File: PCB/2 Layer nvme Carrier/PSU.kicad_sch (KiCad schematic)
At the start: 176 parts, among them J5 Barrel_Jack_Switch, J79 Conn_01x02_Pin, J80 Conn_01x02_Pin, Q5 2N7002, Q6 2N7002, Q7 NCE30P28Q, Q8 2N7002, SW1 SW_Push, SW2 SW_Push, U13 TL431DBZ, U15 SY8253ADC, U16 SY8253ADC, U400 SY8253ADC, U410 SY8253ADC, U420 SY8253ADC, U430 SY8253ADC, U440 SY8253ADC, U450 SY8253ADC, U460 SY8253ADC, U470 SY8253ADC

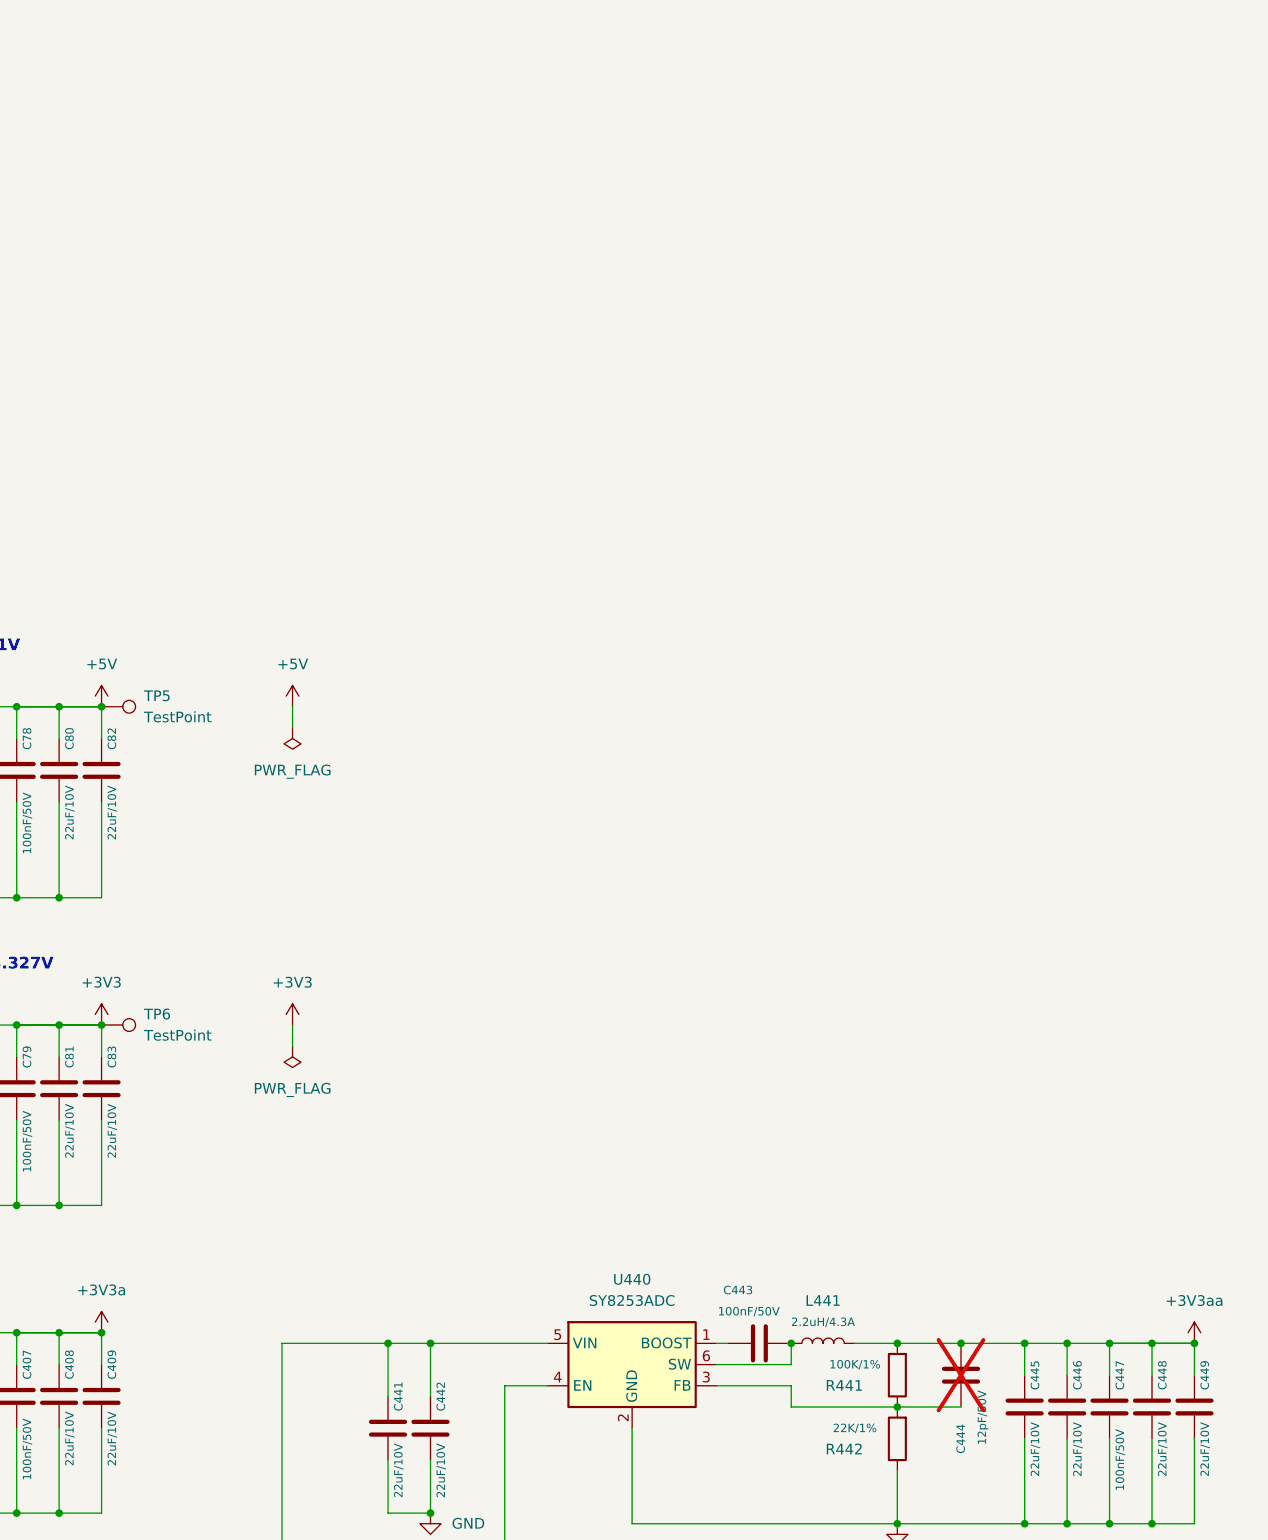
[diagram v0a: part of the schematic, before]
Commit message: Parts change for BOM
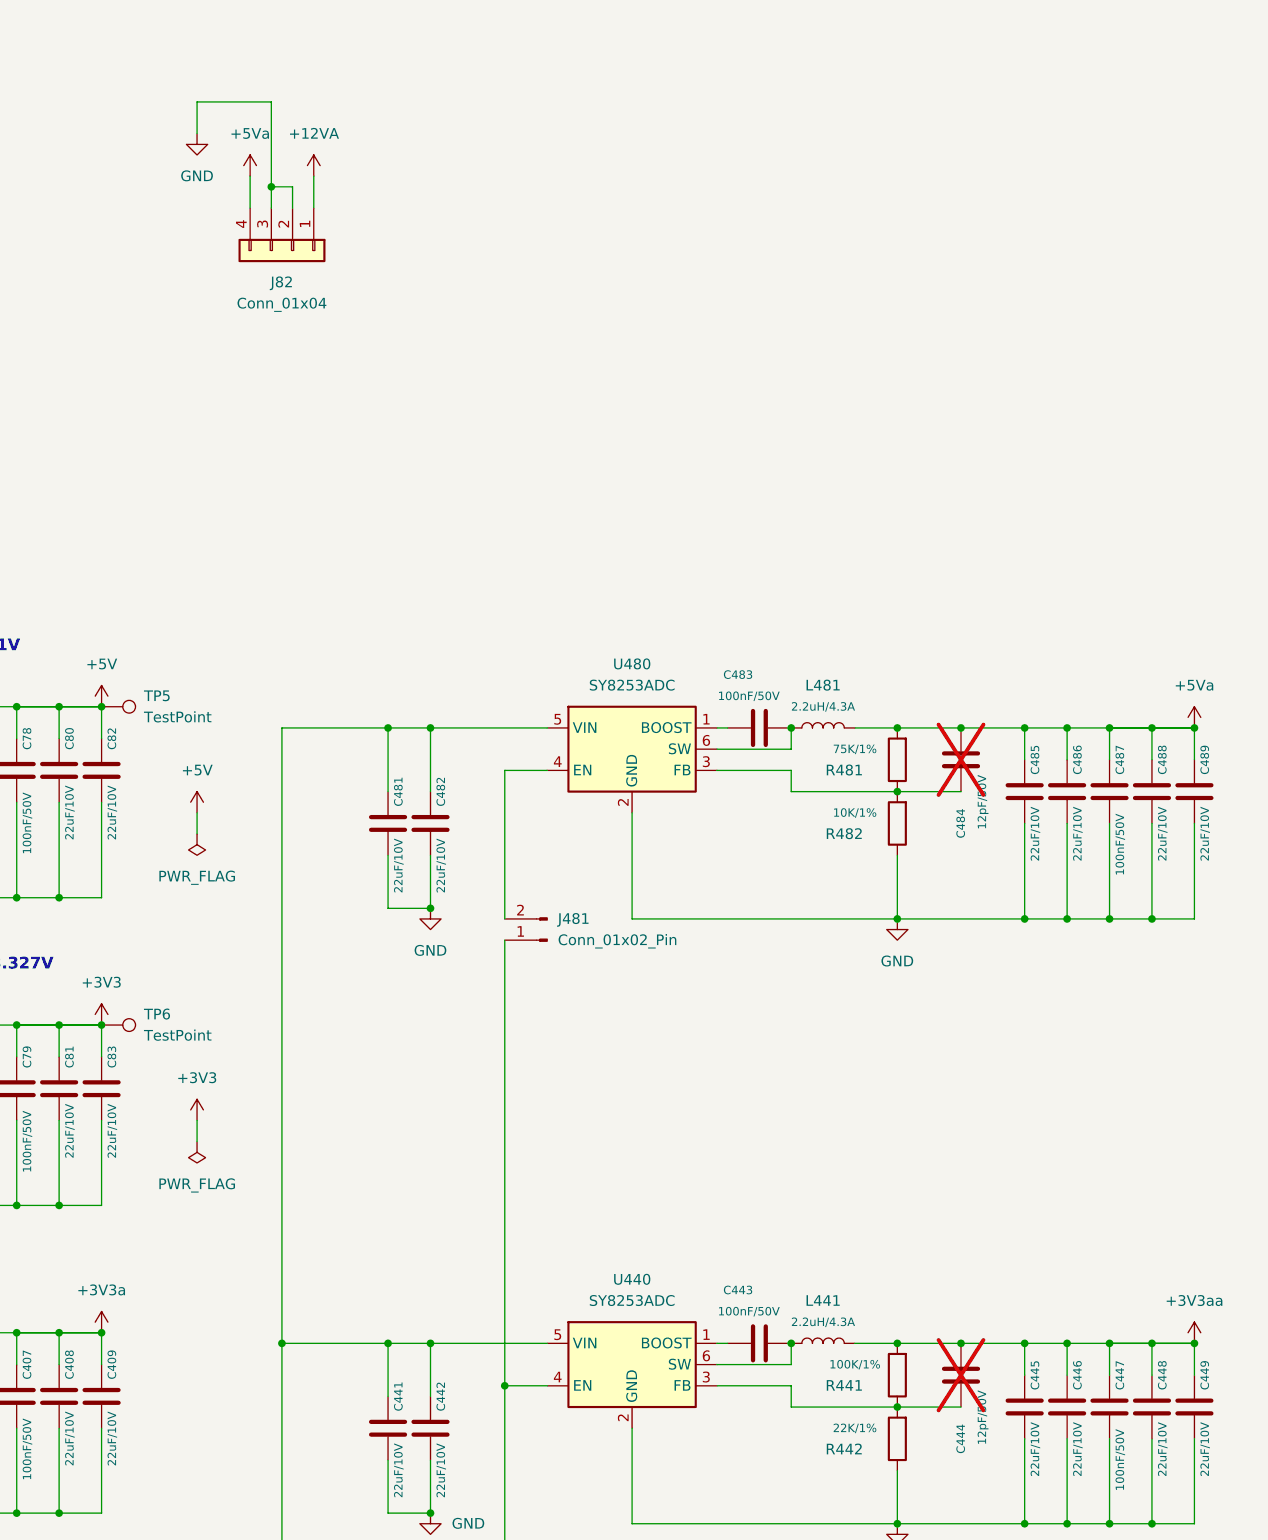
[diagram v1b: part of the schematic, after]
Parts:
- added C481, C482, C485, C486, C488, C489: 22uF/10V, A_HDJ_Library:C_0603_1608Metric, symbol Device:C
- added C483, C487: 100nF/50V, A_HDJ_Library:C_0402_1005Metric, symbol Device:C
- added C484: 12pF/50V, Capacitor_SMD:C_0402_1005Metric, symbol Device:C
- added J481: Conn_01x02_Pin, Connector_PinHeader_2.54mm:PinHeader_1x02_P2.54mm_Vertical, symbol Connector:Conn_01x02_Pin
- added J82: Conn_01x04, Connector_TE-Connectivity:TE_MATE-N-LOK_350211-1_1x04_P5.08mm_Vertical, symbol Connector_Generic:Conn_01x04
- added L481: 2.2uH/4.3A, A_HDJ_Library:L_Sunlord_SWPA4020S, symbol Device:L
- added R481: 75K/1%, A_HDJ_Library:R_0402_1005Metric, symbol Device:R
- added R482: 10K/1%, A_HDJ_Library:R_0402_1005Metric, symbol Device:R
- added U480: SY8253ADC, A_HDJ_Library:TSOT-23-6, symbol Regulator_Switching:LM2734X
- C401, C402, C405, C406, C408, C409, C411, C412, C415, C416, C418, C419, C421, C422, C425, C426, C428, C429, C431, C432, C435, C436, C438, C439, C441, C442, C445, C446, C448, C449, C451, C452, C455, C456, C458, C459, C461, C462, C465, C466, C468, C469, C64, C65, C67, C68, C74, C75, C76, C77, C80, C81, C82, C83: Mfr.# (none) -> CL10A226MP8NUNE
- C403, C407, C413, C417, C423, C427, C433, C437, C443, C447, C453, C457, C463, C467, C70, C71, C78, C79: Mfr.# (none) -> GRM155R71H104KE14D
- C62, C63, C66, C69: Mfr.# (none) -> CL05A105KO5NNNC
- D15, D16, D17: Mfr.# (none) -> SS54
- D21, D25: Mfr.# (none) -> ESD5V0B03-1006
- D22, D23: Mfr.# (none) -> SZYY0603YG
- D24: Mfr.# (none) -> MMS3Z3B3GW
- J5: Mfr.# (none) -> DC007B-2.5-J
- J79, J80: Mfr.# (none) -> 2.54-1*2
- JP1: Mfr.# (none) -> 2.54-1*3
- L1, L2, L401, L411, L421, L431, L441, L451, L461: Mfr.# (none) -> WPN4020H2R2MT
- Q5, Q6, Q8: Mfr.# (none) -> NDS7002A
- Q7: Mfr.# (none) -> NCE30P28Q
- R38, R40, R49, R58: Mfr.# (none) -> RC0402FR-0710KL
- R39, R52, R53: Mfr.# (none) -> RC0402FR-072K2L
- R401, R411, R421, R431, R44, R441, R45, R451, R461, R51, R59: Mfr.# (none) -> RC0402FR-07100KL
- R402, R412, R422, R432, R442, R452, R462, R60: Mfr.# (none) -> RC0402FR-0722KL
- R41, R42, R54: Mfr.# (none) -> RC0402FR-0721K5L
- R46, R48, R55: Mfr.# (none) -> RC0402FR-07100RL
- R47: Mfr.# (none) -> RC0402FR-071KL
- R57: Mfr.# (none) -> RC0402FR-0775KL
- SW1, SW2: Mfr.# (none) -> K2-1102SP-E3SC-04
- U13: Mfr.# (none) -> TL431DBZ
- U15, U16, U400, U410, U420, U430, U440, U450, U460: Mfr.# (none) -> SY8253ADC
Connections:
- net +12VA: now also J82.1 (Pin_1)
- net GND: now also C481.1, C482.1, C485.1, C486.1, C487.2, C488.1, C489.1, J82.2 (Pin_2), J82.3 (Pin_3), R482.1, U480.2 (GND)
- net PWR_EN: now also J481.1 (Pin_1)
- net VDC: now also C481.2, C482.2, U480.5 (VIN)
- new net: C484.2, R481.1, R482.2, U480.3 (FB)
- new net: C483.2, U480.1 (BOOST)
- new net: J481.2 (Pin_2), U480.4 (EN)
- new net: C483.1, L481.1, U480.6 (SW)
- new net +5Va: C484.1, C485.2, C486.2, C487.1, C488.2, C489.2, J82.4 (Pin_4), L481.2, R481.2

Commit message: BOM update and pdf
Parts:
- C401, C402, C405, C406, C408, C409, C411, C412, C415, C416, C418, C419, C421, C422, C425, C426, C428, C429, C431, C432, C435, C436, C438, C439, C441, C442, C445, C446, C448, C449, C451, C452, C455, C456, C458, C459, C461, C462, C465, C466, C468, C469, C481, C482, C485, C486, C488, C489, C64, C65, C67, C68, C74, C75, C76, C77, C80, C81, C82, C83: MPN (none) -> CL10A226MP8NUNE; Mfr.# CL10A226MP8NUNE -> (none)
- C403, C407, C413, C417, C423, C427, C433, C437, C443, C447, C453, C457, C463, C467, C483, C487, C70, C71, C78, C79: MPN (none) -> GRM155R71H104KE14D; Mfr.# GRM155R71H104KE14D -> (none)
- C62, C63, C66, C69: MPN (none) -> CL05A105KO5NNNC; Mfr.# CL05A105KO5NNNC -> (none)
- D15, D16, D17: MPN (none) -> SS54; Mfr.# SS54 -> (none)
- D21, D25: MPN (none) -> ESD5V0B03-1006; Mfr.# ESD5V0B03-1006 -> (none)
- D22, D23: MPN (none) -> SZYY0603YG; Mfr.# SZYY0603YG -> (none)
- D24: MPN (none) -> MMS3Z3B3GW; Mfr.# MMS3Z3B3GW -> (none)
- J481, J79, J80: MPN (none) -> 2.54-1*2; Mfr.# 2.54-1*2 -> (none)
- J5: MPN (none) -> DC007B-2.5-J; Mfr.# DC007B-2.5-J -> (none)
- J82: MPN (none) -> 770997-1; Mfr.# 770997-1 -> (none)
- JP1: MPN (none) -> 2.54-1*3; Mfr.# 2.54-1*3 -> (none)
- L1, L2, L401, L411, L421, L431, L441, L451, L461, L481: MPN (none) -> WPN4020H2R2MT; Mfr.# WPN4020H2R2MT -> (none)
- Q5, Q6, Q8: MPN (none) -> NDS7002A; Mfr.# NDS7002A -> (none)
- Q7: MPN (none) -> NCE30P28Q; Mfr.# NCE30P28Q -> (none)
- R38, R40, R482, R49, R58: MPN (none) -> RC0402FR-0710KL; Mfr.# RC0402FR-0710KL -> (none)
- R39, R52, R53: MPN (none) -> RC0402FR-072K2L; Mfr.# RC0402FR-072K2L -> (none)
- R401, R411, R421, R431, R44, R441, R45, R451, R461, R51, R59: MPN (none) -> RC0402FR-07100KL; Mfr.# RC0402FR-07100KL -> (none)
- R402, R412, R422, R432, R442, R452, R462, R60: MPN (none) -> RC0402FR-0722KL; Mfr.# RC0402FR-0722KL -> (none)
- R41, R42, R54: MPN (none) -> RC0402FR-0721K5L; Mfr.# RC0402FR-0721K5L -> (none)
- R46, R48, R55: MPN (none) -> RC0402FR-07100RL; Mfr.# RC0402FR-07100RL -> (none)
- R47: MPN (none) -> RC0402FR-071KL; Mfr.# RC0402FR-071KL -> (none)
- R481, R57: MPN (none) -> RC0402FR-0775KL; Mfr.# RC0402FR-0775KL -> (none)
- SW1, SW2: MPN (none) -> K2-1102SP-E3SC-04; Mfr.# K2-1102SP-E3SC-04 -> (none)
- U13: MPN (none) -> TL431DBZ; Mfr.# TL431DBZ -> (none)
- U15, U16, U400, U410, U420, U430, U440, U450, U460, U480: MPN (none) -> SY8253ADC; Mfr.# SY8253ADC -> (none)

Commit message: Rework for PSU and REFCLK
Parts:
- removed C62, C63: 1uF/16V, A_HDJ_Library:C_0402_1005Metric, symbol Device:C
- removed D15, D16, D17: SS54, A_HDJ_Library:D_SMA, symbol Device:D_Schottky
- removed JP1: Jumper_3_Bridged12, A_HDJ_Library:PinHeader_1x03_P2.54mm_Vertical, symbol Jumper:Jumper_3_Bridged12
- removed Q5, Q6: 2N7002, A_HDJ_Library:SOT-23, symbol Transistor_FET:2N7002
- removed Q7: NCE30P28Q, A_HDJ_Library:MOSFET_PDFN8_3.3x3.3, symbol A_HDJ_Library:AON7262E
- removed R38, R40: 10K/1%, A_HDJ_Library:R_0402_1005Metric, symbol Device:R
- removed R39: 2.2K/1%, A_HDJ_Library:R_0402_1005Metric, symbol Device:R
- removed R41, R42: 21.5K/1%, A_HDJ_Library:R_0402_1005Metric, symbol Device:R
- removed R44, R45: 100K/1%, A_HDJ_Library:R_0402_1005Metric, symbol Device:R
- removed TP8, TP9: TestPoint, A_HDJ_Library:TestPoint_Pad_D1.5mm, symbol Connector:TestPoint
- removed U13: TL431DBZ, A_HDJ_Library:SOT-23, symbol Reference_Voltage:TL431DBZ
- added D81: PTVS12VP1UP, Diode_SMD_AKL:D_SOD-128, symbol PCM_Diode_TVS_AKL:PTVS12VP1UP
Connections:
- net +12VA is gone; now on net +12V: J82.1 (Pin_1), R54.1
- net VDC is gone; now on net +12V: C401.2, C402.2, C411.2, C412.2, C421.2, C422.2, C431.2, C432.2, C441.2, C442.2, C451.2, C452.2, C461.2, C462.2, C471.2, C472.2, C481.2, C482.2, C64.2, C65.2, C67.2, C68.2, R53.1, U15.5 (VIN), U16.5 (VIN), U400.5 (VIN), U410.5 (VIN), U420.5 (VIN), U430.5 (VIN), U440.5 (VIN), U450.5 (VIN), U460.5 (VIN), U470.5 (VIN), U480.5 (VIN)
- net +12V: now also D81.1 (K)
- net GND: now also D81.2 (A)
- net ~{PWR_LED}/~{PSON}: now also R46.1
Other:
- note removed: "PCIe Power Enable LED"
- note removed: "Power for PCIe x4 OVP@13.86V"
- note removed: "soft start"
- moved on the sheet: J82, TP4

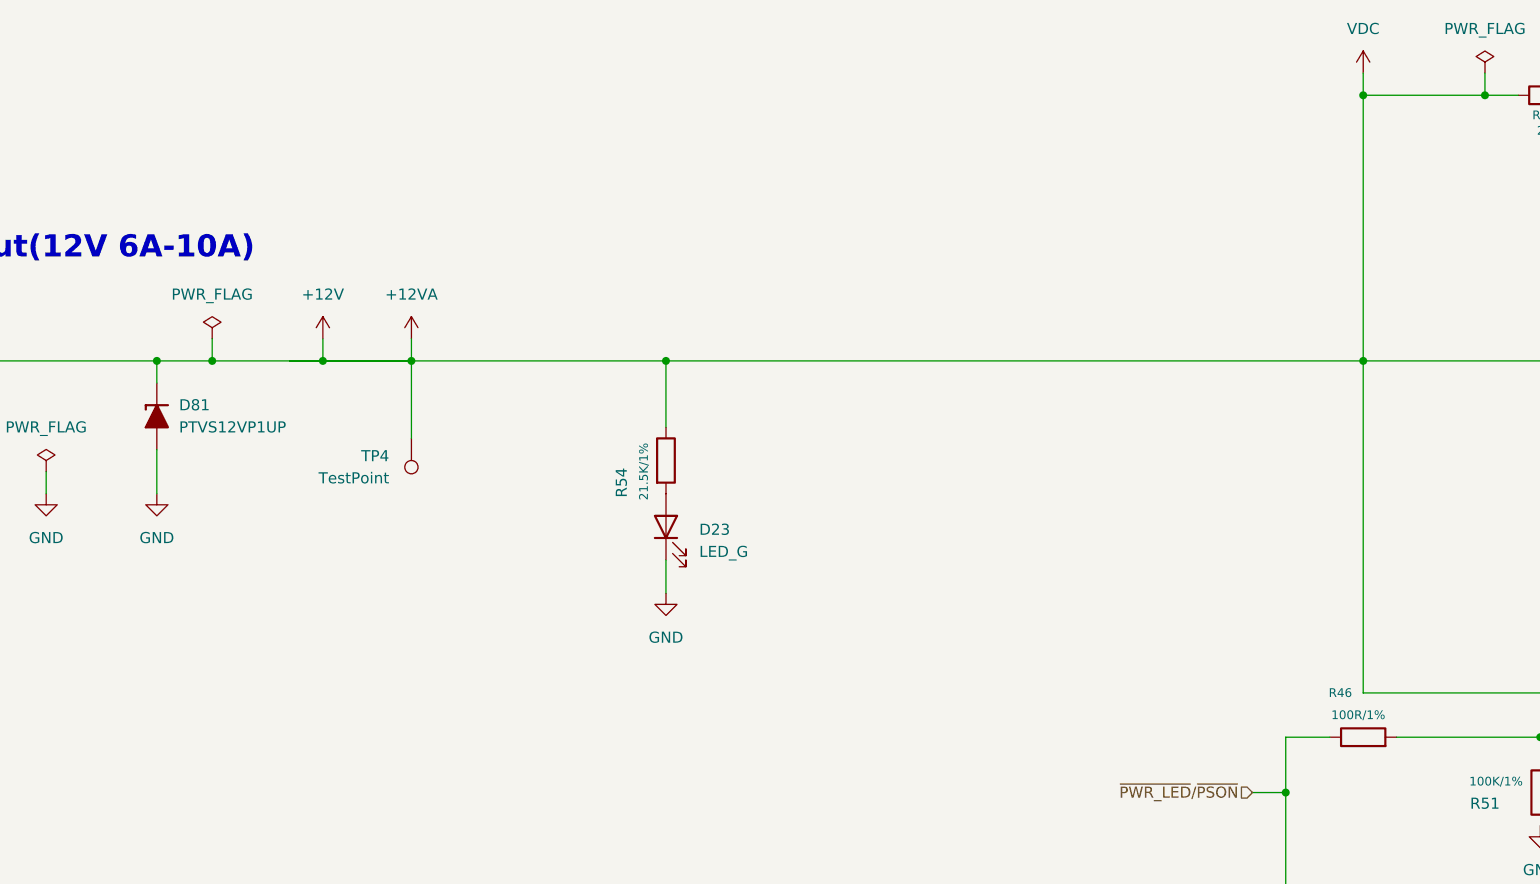
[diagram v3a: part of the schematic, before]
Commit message: change to 12V and more work to do
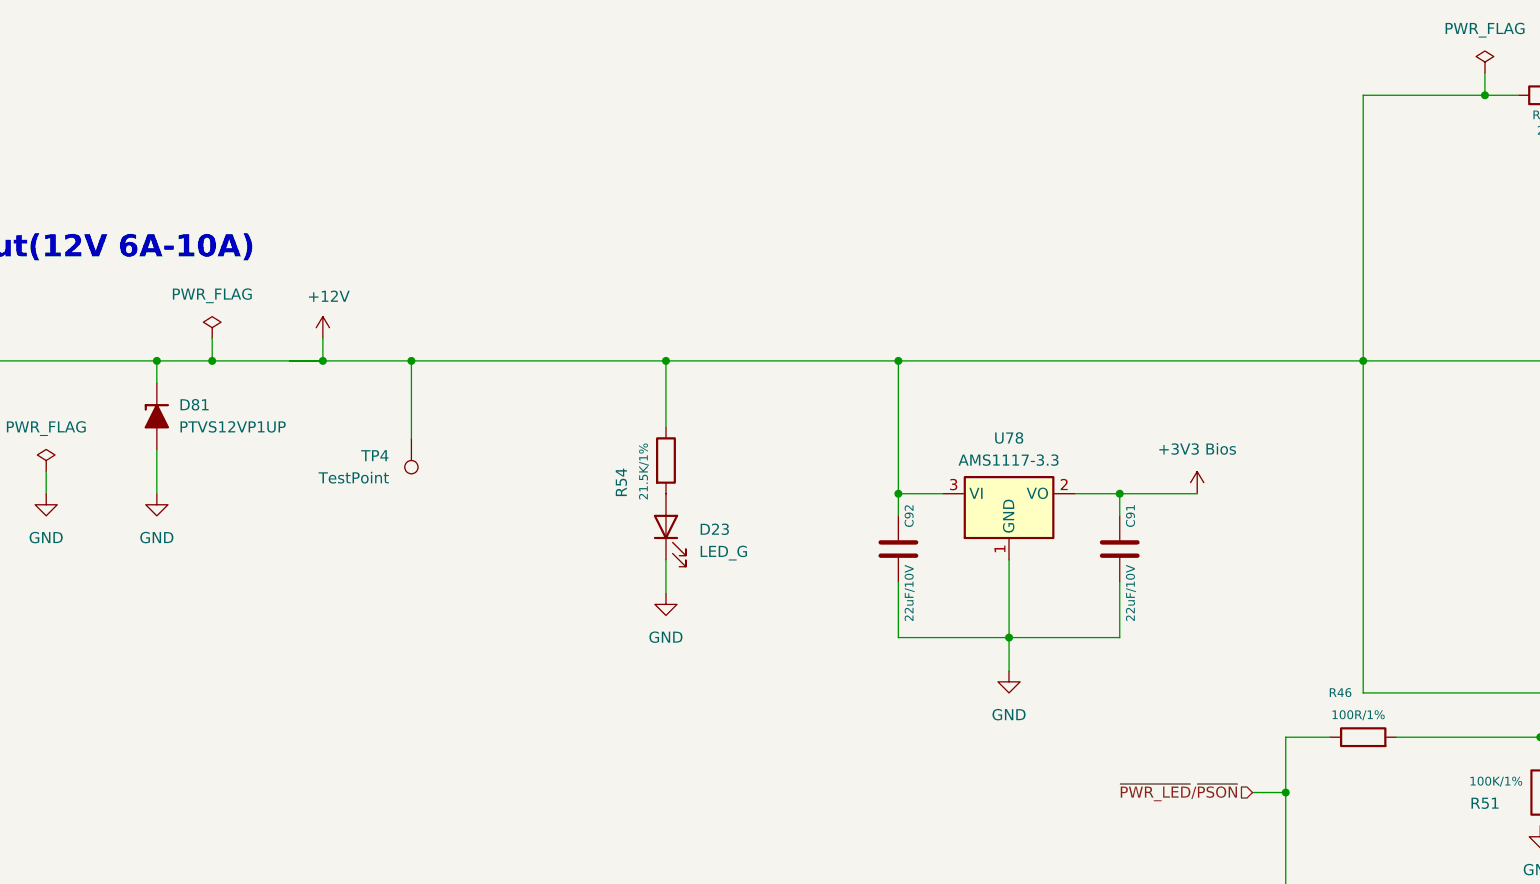
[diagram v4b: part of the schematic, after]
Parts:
- added C91, C92: 22uF/10V, A_HDJ_Library:C_0603_1608Metric, symbol Device:C
- added U78: AMS1117-3.3, Package_TO_SOT_SMD:SOT-223-3_TabPin2, symbol Regulator_Linear:AMS1117-3.3
- J79, J80: MPN 2.54-1*2 -> PZ2.54-1*2
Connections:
- net +12V: now also C92.2, U78.3 (VI)
- net GND: now also C91.1, C92.1, U78.1 (GND)
- new net +3V3 Bios: C91.2, U78.2 (VO)

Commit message: Rework started with PCIe
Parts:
- D81: footprint Diode_SMD_AKL:D_SOD-128 -> Diode_SMD:D_SOD-128
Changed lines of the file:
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@@
 			)
 		)
-		(property "Footprint" "Diode_SMD_AKL:D_SOD-128"
+		(property "Footprint" "Diode_SMD:D_SOD-128"
 			(at 92.71 111.76 0)
 			(effects
